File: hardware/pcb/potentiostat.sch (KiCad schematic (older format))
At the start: 94 parts, among them K1 CONN_3, P1 CONN_2, P10 CONN_2, P11 CONN_2, P12 CONN_2, P13 CONN_5X2, P14 CONN_5X2, P15 CONN_2X2, P16 CONN_2X2, P17 CONN_2, P18 CONN_2, P19 CONN_2, P2 CONN_2, P20 CONN_2, P21 CONN_2, P3 CONN_2, P4 CONN_2, P5 CONN_2, P6 CONN_2, P7 CONN_2, P8 CONN_2, P9 CONN_2, U1 ZXRE060, U10 OPA227, U11 OP07, U12 LT1995, U13 ADG44X, U2 TEENSY3.1, U3 MAX6176AASA+, U4 LT1995, U5 AD8250, U6 MEA1D05XXSC, U7 OPA129, U8 OPA129, U9 ADG44X

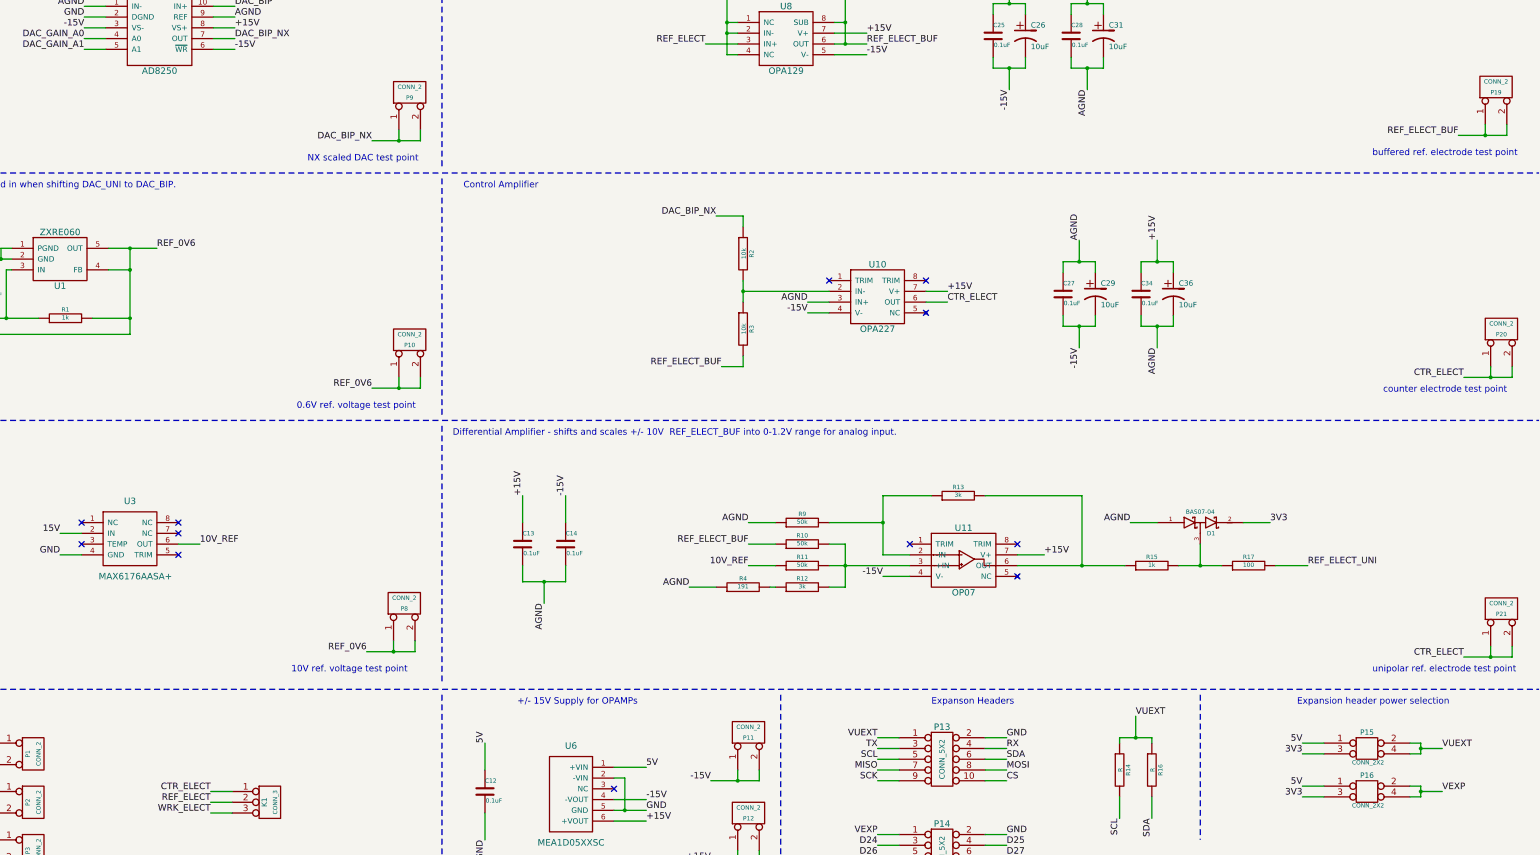
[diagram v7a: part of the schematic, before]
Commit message: Finished footprint assignment. Worked on PCB layout.
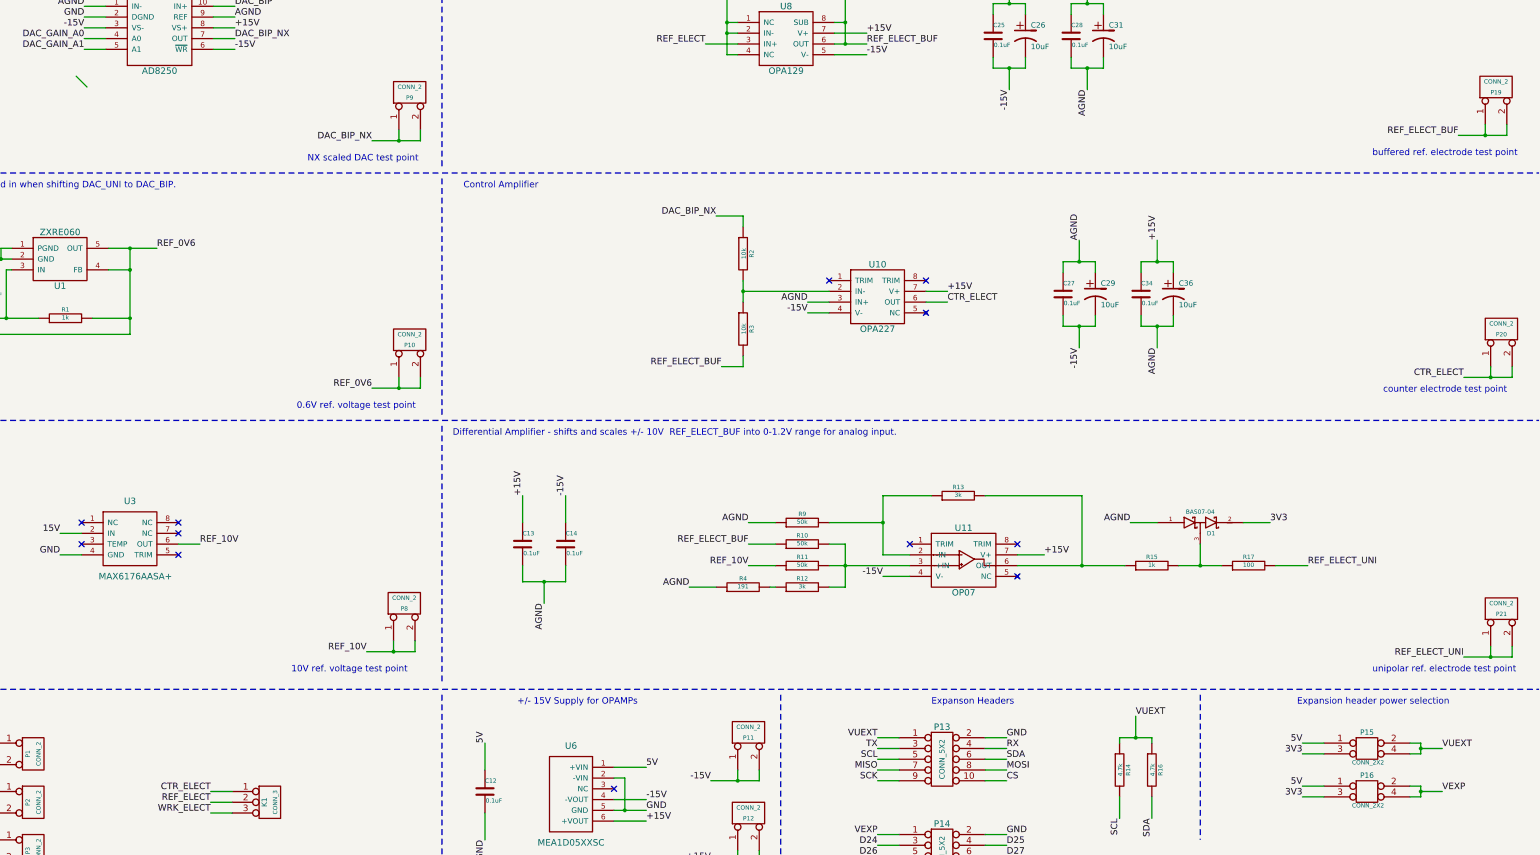
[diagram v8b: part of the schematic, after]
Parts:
- R14, R16: value R -> 4.7k
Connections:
- net CTR_ELECT: no longer P21.1 (P1), P21.2 (PM)
- net REF_0V6: no longer P8.1 (P1), P8.2 (PM)
- net REF_ELECT_UNI: now also P21.1 (P1), P21.2 (PM)
- net 10V_REF renamed REF_10V
- net REF_10V: now also P8.1 (P1), P8.2 (PM)
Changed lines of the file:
@@
 Sheet 1 1
 Title ""
-Date "16 nov 2016"
+Date "17 nov 2016"
 Rev ""
 Comp ""
@@
 Connection ~ 16050 13700
 Text Label 15800 13700 2    60   ~ 0
-CTR_ELECT
+REF_ELECT_UNI
 Text Notes 14950 13850 0    60   ~ 0
 unipolar ref. electrode test point
@@
 GND
 Text Label 4050 12650 0    60   ~ 0
-10V_REF
+REF_10V
 $Comp
 L CONN_2 P8
@@
 Connection ~ 5850 13650
 Text Label 5600 13650 2    60   ~ 0
-REF_0V6
+REF_10V
 Text Notes 4900 13850 0    60   ~ 0
 10V ref. voltage test point
@@
 	9400 12450 9150 12450
 Text Label 9150 12850 2    60   ~ 0
-10V_REF
+REF_10V
 Text Label 9150 12450 2    60   ~ 0
 AGND
@@
 P 12600 14750
 F 0 "R14" V 12680 14750 40  0000 C CNN
-F 1 "R" V 12607 14751 40  0000 C CNN
+F 1 "4.7k" V 12607 14751 40  0000 C CNN
 F 2 "~" V 12530 14750 30  0000 C CNN
 F 3 "~" H 12600 14750 30  0000 C CNN
@@
 P 12900 14750
 F 0 "R16" V 12980 14750 40  0000 C CNN
-F 1 "R" V 12907 14751 40  0000 C CNN
+F 1 "4.7k" V 12907 14751 40  0000 C CNN
 F 2 "~" V 12830 14750 30  0000 C CNN
 F 3 "~" H 12900 14750 30  0000 C CNN
@@
 Text Notes 11150 4900 0    60   ~ 0
 Use ADG441
+Entry Wire Line
+	2900 8300 3000 8400
 $EndSCHEMATC
